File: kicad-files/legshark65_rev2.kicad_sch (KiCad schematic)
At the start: 193 parts, among them J1 ARM JTAG, J2 Conn_01x04, SW1 K2-1187SQ-A4SW-06, SW2 PCM12SMTR, T2 53261-0471, U1 STM32F411CEU6, U2 MCP1700T-3302E/TT, U3 AT24C256C-SSHL-T, Y1 TAXM8M4RFDCET2T

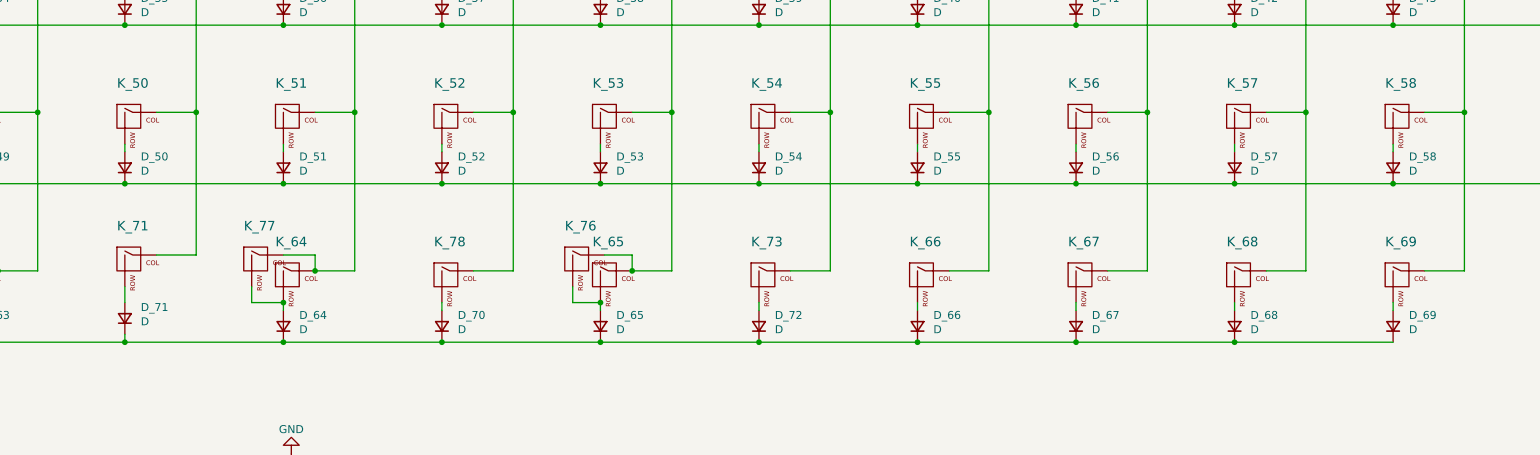
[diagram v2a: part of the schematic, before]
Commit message: Added alternate mods to the right side
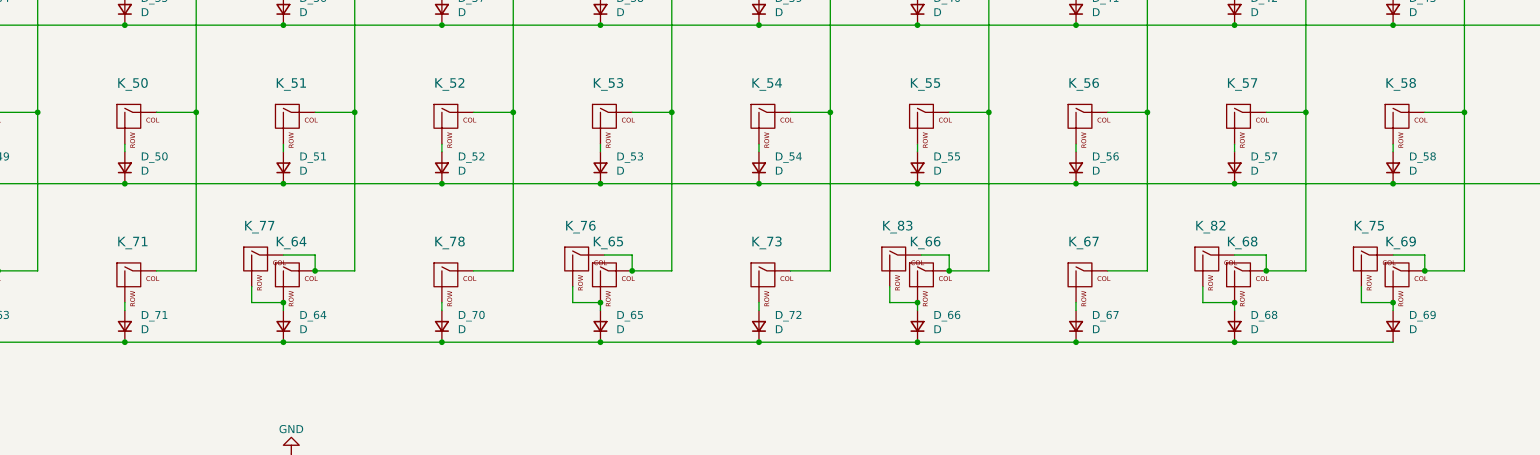
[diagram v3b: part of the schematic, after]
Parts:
- added K_75, K_83: KEYSW, MX_Only:MXOnly-1.5U-NoLED, symbol MX_Alps_Hybrid:MX-NoLED
- added K_82: KEYSW, MX_Only:MXOnly-1U-NoLED, symbol MX_Alps_Hybrid:MX-NoLED
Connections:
- net col10: now also K_83.1 (COL)
- net col12: now also K_82.1 (COL)
- net col13: now also K_75.1 (COL)
- net at D_68.2 (A), K_68.2 (ROW): now also K_82.2 (ROW)
- net at D_66.2 (A), K_66.2 (ROW): now also K_83.2 (ROW)
- net at D_69.2 (A), K_69.2 (ROW): now also K_75.2 (ROW)
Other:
- moved on the sheet: D_71, K_71
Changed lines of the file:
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@@
   (junction (at 223.52 100.33) (diameter 0) (color 0 0 0 0)
   )
+  (junction (at 364.49 130.81) (diameter 0) (color 0 0 0 0)
+  )
   (junction (at 186.69 60.96) (diameter 0) (color 0 0 0 0)
   )
@@
   (junction (at 110.49 35.56) (diameter 0) (color 0 0 0 0)
   )
+  (junction (at 339.09 130.81) (diameter 0) (color 0 0 0 0)
+  )
   (junction (at 191.77 125.73) (diameter 0) (color 0 0 0 0)
   )
@@
   (junction (at 375.92 100.33) (diameter 0) (color 0 0 0 0)
   )
+  (junction (at 369.57 125.73) (diameter 0) (color 0 0 0 0)
+  )
   (junction (at 110.49 60.96) (diameter 0) (color 0 0 0 0)
   )
@@
   (junction (at 313.69 86.36) (diameter 0) (color 0 0 0 0)
   )
+  (junction (at 288.29 130.81) (diameter 0) (color 0 0 0 0)
+  )
   (junction (at 161.29 35.56) (diameter 0) (color 0 0 0 0)
   )
@@
   (junction (at 401.32 49.53) (diameter 0) (color 0 0 0 0)
   )
+  (junction (at 293.37 125.73) (diameter 0) (color 0 0 0 0)
+  )
   (junction (at 135.89 86.36) (diameter 0) (color 0 0 0 0)
   )
@@
   (junction (at 172.72 74.93) (diameter 0) (color 0 0 0 0)
   )
+  (junction (at 344.17 125.73) (diameter 0) (color 0 0 0 0)
+  )
   (junction (at 299.72 74.93) (diameter 0) (color 0 0 0 0)
   )
@@
     (stroke (width 0) (type default))
   )
-  (wire (pts (xy 161.29 128.27) (xy 161.29 130.81))
+  (wire (pts (xy 161.29 130.81) (xy 161.29 132.08))
     (stroke (width 0) (type default))
   )
@@
     (stroke (width 0) (type default))
   )
-  (wire (pts (xy 166.37 123.19) (xy 172.72 123.19))
+  (wire (pts (xy 166.37 125.73) (xy 172.72 125.73))
     (stroke (width 0) (type default))
   )
@@
     (stroke (width 0) (type default))
   )
+  (wire (pts (xy 359.41 128.27) (xy 359.41 130.81))
+    (stroke (width 0) (type default))
+  )
   (wire (pts (xy 198.12 125.73) (xy 198.12 100.33))
     (stroke (width 0) (type default))
@@
     (stroke (width 0) (type default))
   )
+  (wire (pts (xy 283.845 130.81) (xy 288.29 130.81))
+    (stroke (width 0) (type default))
+  )
   (wire (pts (xy 142.24 180.975) (xy 142.24 187.96))
     (stroke (width 0) (type default))
@@
     (stroke (width 0) (type default))
   )
-  (wire (pts (xy 172.72 123.19) (xy 172.72 100.33))
+  (wire (pts (xy 172.72 125.73) (xy 172.72 100.33))
     (stroke (width 0) (type default))
   )
@@
     (stroke (width 0) (type default))
   )
+  (wire (pts (xy 369.57 123.19) (xy 369.57 125.73))
+    (stroke (width 0) (type default))
+  )
   (wire (pts (xy 47.625 259.715) (xy 50.165 259.715))
     (stroke (width 0) (type default))
@@
     (stroke (width 0) (type default))
   )
+  (wire (pts (xy 364.49 123.19) (xy 369.57 123.19))
+    (stroke (width 0) (type default))
+  )
   (wire (pts (xy 267.97 100.33) (xy 274.32 100.33))
     (stroke (width 0) (type default))
@@
     (stroke (width 0) (type default))
   )
+  (wire (pts (xy 334.01 130.81) (xy 339.09 130.81))
+    (stroke (width 0) (type default))
+  )
   (wire (pts (xy 135.89 35.56) (xy 161.29 35.56))
     (stroke (width 0) (type default))
@@
     (stroke (width 0) (type default))
   )
+  (wire (pts (xy 344.17 123.19) (xy 344.17 125.73))
+    (stroke (width 0) (type default))
+  )
   (wire (pts (xy 191.77 283.21) (xy 191.77 285.75))
     (stroke (width 0) (type default))
@@
     (stroke (width 0) (type default))
   )
+  (wire (pts (xy 334.01 128.27) (xy 334.01 130.81))
+    (stroke (width 0) (type default))
+  )
   (wire (pts (xy 344.17 24.13) (xy 350.52 24.13))
     (stroke (width 0) (type default))
@@
     (stroke (width 0) (type default))
   )
+  (wire (pts (xy 283.845 128.27) (xy 283.845 130.81))
+    (stroke (width 0) (type default))
+  )
   (wire (pts (xy 81.28 156.21) (xy 77.47 156.21))
     (stroke (width 0) (type default))
@@
     (stroke (width 0) (type default))
   )
+  (wire (pts (xy 293.37 123.19) (xy 293.37 125.73))
+    (stroke (width 0) (type default))
+  )
   (wire (pts (xy 318.77 100.33) (xy 325.12 100.33))
     (stroke (width 0) (type default))
@@
     (stroke (width 0) (type default))
   )
-  (wire (pts (xy 161.29 135.89) (xy 161.29 137.16))
-    (stroke (width 0) (type default))
-  )
   (wire (pts (xy 191.77 125.73) (xy 198.12 125.73))
     (stroke (width 0) (type default))
@@
     (stroke (width 0) (type default))
   )
+  (wire (pts (xy 359.41 130.81) (xy 364.49 130.81))
+    (stroke (width 0) (type default))
+  )
   (wire (pts (xy 64.77 24.13) (xy 71.12 24.13))
     (stroke (width 0) (type default))
@@
     (stroke (width 0) (type default))
   )
+  (wire (pts (xy 339.09 123.19) (xy 344.17 123.19))
+    (stroke (width 0) (type default))
+  )
   (wire (pts (xy 262.89 137.16) (xy 288.29 137.16))
     (stroke (width 0) (type default))
@@
     (stroke (width 0) (type default))
   )
+  (wire (pts (xy 288.925 123.19) (xy 293.37 123.19))
+    (stroke (width 0) (type default))
+  )
   (wire (pts (xy 204.47 283.21) (xy 204.47 298.45))
     (stroke (width 0) (type default))
@@
     )
   )
-  (symbol (lib_id "MX_Alps_Hybrid:MX-NoLED") (at 162.56 124.46 0) (unit 1)
+  (symbol (lib_id "MX_Alps_Hybrid:MX-NoLED") (at 162.56 127 0) (unit 1)
     (in_bom yes) (on_board yes) (dnp no)
-    (property "Reference" "K_71" (at 162.56 118.5418 0)
+    (property "Reference" "K_71" (at 162.56 121.0818 0)
       (effects (font (size 1.524 1.524)))
     )
-    (property "Value" "KEYSW" (at 162.56 127 0)
+    (property "Value" "KEYSW" (at 162.56 129.54 0)
       (effects (font (size 1.524 1.524)) hide)
     )
-    (property "Footprint" "MX_Only:MXOnly-1U-NoLED" (at 162.56 124.46 0)
+    (property "Footprint" "MX_Only:MXOnly-1U-NoLED" (at 162.56 127 0)
       (effects (font (size 1.524 1.524)) hide)
     )
-    (property "Datasheet" "" (at 162.56 124.46 0)
+    (property "Datasheet" "" (at 162.56 127 0)
       (effects (font (size 1.524 1.524)))
     )
@@
     )
   )
+  (symbol (lib_id "MX_Alps_Hybrid:MX-NoLED") (at 360.68 124.46 0) (unit 1)
+    (in_bom yes) (on_board yes) (dnp no)
+    (property "Reference" "K_75" (at 360.68 118.5418 0)
+      (effects (font (size 1.524 1.524)))
+    )
+    (property "Value" "KEYSW" (at 360.68 127 0)
+      (effects (font (size 1.524 1.524)) hide)
+    )
+    (property "Footprint" "MX_Only:MXOnly-1.5U-NoLED" (at 360.68 124.46 0)
+      (effects (font (size 1.524 1.524)) hide)
+    )
+    (property "Datasheet" "" (at 360.68 124.46 0)
+      (effects (font (size 1.524 1.524)))
+    )
+    (pin "1")
+    (pin "2")
+    (instances
+      (project "legshark65_rev2"
+        (path "/2fcc1073-d3f4-43f9-b3b4-5cee13272705"
+          (reference "K_75") (unit 1)
+        )
+      )
+    )
+  )
   (symbol (lib_id "MX_Alps_Hybrid:MX-NoLED") (at 81.915 124.46 0) (unit 1)
     (in_bom yes) (on_board yes) (dnp no)
@@
     )
   )
-  (symbol (lib_id "Device:D_Small") (at 161.29 133.35 90) (unit 1)
+  (symbol (lib_id "Device:D_Small") (at 161.29 134.62 90) (unit 1)
     (in_bom yes) (on_board yes) (dnp no)
-    (property "Reference" "D_71" (at 163.83 131.572 90)
+    (property "Reference" "D_71" (at 163.83 132.842 90)
       (effects (font (size 1.27 1.27)) (justify right))
     )
-    (property "Value" "D" (at 163.83 133.858 90)
+    (property "Value" "D" (at 163.83 135.128 90)
       (effects (font (size 1.27 1.27)) (justify right))
     )
-    (property "Footprint" "Diode_SMD:D_SOD-523" (at 162.56 140.97 0)
+    (property "Footprint" "Diode_SMD:D_SOD-523" (at 162.56 142.24 0)
       (effects (font (size 1.27 1.27)) hide)
     )
-    (property "Datasheet" "~" (at 162.56 140.97 0)
+    (property "Datasheet" "~" (at 162.56 142.24 0)
       (effects (font (size 1.27 1.27)) hide)
     )
@@
     )
   )
+  (symbol (lib_id "MX_Alps_Hybrid:MX-NoLED") (at 335.28 124.46 0) (unit 1)
+    (in_bom yes) (on_board yes) (dnp no)
+    (property "Reference" "K_82" (at 335.28 118.5418 0)
+      (effects (font (size 1.524 1.524)))
+    )
+    (property "Value" "KEYSW" (at 335.28 127 0)
+      (effects (font (size 1.524 1.524)) hide)
+    )
+    (property "Footprint" "MX_Only:MXOnly-1U-NoLED" (at 335.28 124.46 0)
+      (effects (font (size 1.524 1.524)) hide)
+    )
+    (property "Datasheet" "" (at 335.28 124.46 0)
+      (effects (font (size 1.524 1.524)))
+    )
+    (pin "1")
+    (pin "2")
+    (instances
+      (project "legshark65_rev2"
+        (path "/2fcc1073-d3f4-43f9-b3b4-5cee13272705"
+          (reference "K_82") (unit 1)
+        )
+      )
+    )
+  )
   (symbol (lib_id "MX_Alps_Hybrid:MX-NoLED") (at 187.96 127 0) (unit 1)
     (in_bom yes) (on_board yes) (dnp no)
@@
         )
       )
+    )
+  )
+  (symbol (lib_id "MX_Alps_Hybrid:MX-NoLED") (at 285.115 124.46 0) (unit 1)
+    (in_bom yes) (on_board yes) (dnp no)
+    (property "Reference" "K_83" (at 285.115 118.5418 0)
+      (effects (font (size 1.524 1.524)))
+    )
+    (property "Value" "KEYSW" (at 285.115 127 0)
+      (effects (font (size 1.524 1.524)) hide)
+    )
+    (property "Footprint" "MX_Only:MXOnly-1.5U-NoLED" (at 285.115 124.46 0)
+      (effects (font (size 1.524 1.524)) hide)
+    )
+    (property "Datasheet" "" (at 285.115 124.46 0)
+      (effects (font (size 1.524 1.524)))
+    )
+    (pin "1")
+    (pin "2")
+    (instances
+      (project "legshark65_rev2"
+        (path "/2fcc1073-d3f4-43f9-b3b4-5cee13272705"
+          (reference "K_83") (unit 1)
+        )
+      )

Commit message: Added 3U stabs to the 7U footprint for even more layout support
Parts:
- K_78: footprint MX_Only:MXOnly-7U-ReversedStabilizers-NoLED -> Legshark:Legshark_MXOnly-7U-3U-ReversedStabilizers-NoLED
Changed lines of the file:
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@@
       (effects (font (size 1.524 1.524)) hide)
     )
-    (property "Footprint" "MX_Only:MXOnly-7U-ReversedStabilizers-NoLED" (at 213.36 127 0)
+    (property "Footprint" "Legshark:Legshark_MXOnly-7U-3U-ReversedStabilizers-NoLED" (at 213.36 127 0)
       (effects (font (size 1.524 1.524)) hide)
     )

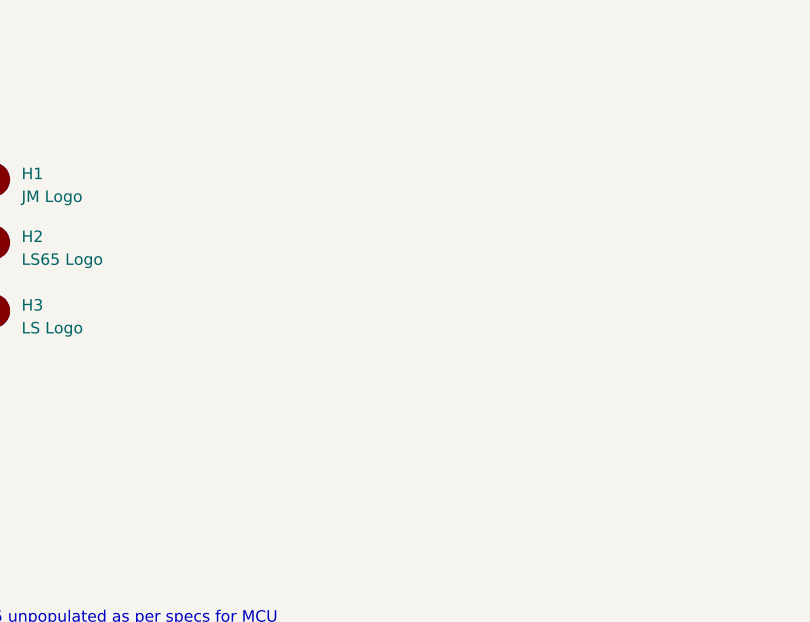
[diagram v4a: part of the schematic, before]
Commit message: added mounting holes with clearence
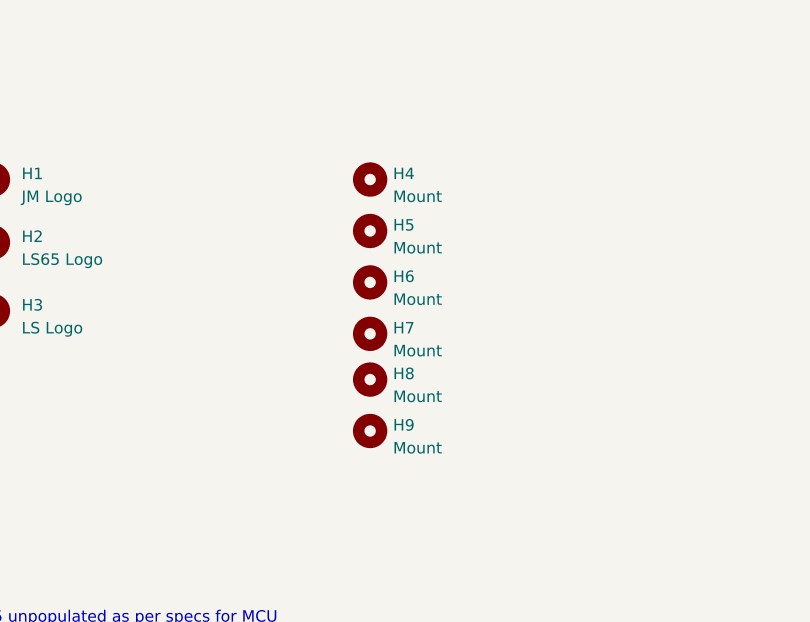
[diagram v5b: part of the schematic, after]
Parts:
- added H4, H5, H6, H7, H8, H9: Mount, MountingHole:MountingHole_3.2mm_M3_ISO14580, symbol Mechanical:MountingHole
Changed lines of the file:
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@@
     )
   )
+  (symbol (lib_id "Mechanical:MountingHole") (at 285.75 191.77 0) (unit 1)
+    (in_bom yes) (on_board yes) (dnp no) (fields_autoplaced)
+    (property "Reference" "H7" (at 288.29 191.135 0)
+      (effects (font (size 1.27 1.27)) (justify left))
+    )
+    (property "Value" "Mount" (at 288.29 193.675 0)
+      (effects (font (size 1.27 1.27)) (justify left))
+    )
+    (property "Footprint" "MountingHole:MountingHole_3.2mm_M3_ISO14580" (at 285.75 191.77 0)
+      (effects (font (size 1.27 1.27)) hide)
+    )
+    (property "Datasheet" "~" (at 285.75 191.77 0)
+      (effects (font (size 1.27 1.27)) hide)
+    )
+    (instances
+      (project "legshark65_rev2"
+        (path "/2fcc1073-d3f4-43f9-b3b4-5cee13272705"
+          (reference "H7") (unit 1)
+        )
+      )
+      (project "legshark65_rev1"
+        (path "/9ddf6dc5-8b5e-413a-9b25-d1d5a5a60469"
+          (reference "H3") (unit 1)
+        )
+      )
+    )
+  )
   (symbol (lib_id "Device:D_Small") (at 85.09 134.62 90) (unit 1)
     (in_bom yes) (on_board yes) (dnp no)
@@
     )
   )
+  (symbol (lib_id "Mechanical:MountingHole") (at 285.75 202.565 0) (unit 1)
+    (in_bom yes) (on_board yes) (dnp no) (fields_autoplaced)
+    (property "Reference" "H9" (at 288.29 201.93 0)
+      (effects (font (size 1.27 1.27)) (justify left))
+    )
+    (property "Value" "Mount" (at 288.29 204.47 0)
+      (effects (font (size 1.27 1.27)) (justify left))
+    )
+    (property "Footprint" "MountingHole:MountingHole_3.2mm_M3_ISO14580" (at 285.75 202.565 0)
+      (effects (font (size 1.27 1.27)) hide)
+    )
+    (property "Datasheet" "~" (at 285.75 202.565 0)
+      (effects (font (size 1.27 1.27)) hide)
+    )
+    (instances
+      (project "legshark65_rev2"
+        (path "/2fcc1073-d3f4-43f9-b3b4-5cee13272705"
+          (reference "H9") (unit 1)
+        )
+      )
+      (project "legshark65_rev1"
+        (path "/9ddf6dc5-8b5e-413a-9b25-d1d5a5a60469"
+          (reference "H3") (unit 1)
+        )
+      )
+    )
+  )
   (symbol (lib_id "MX_Alps_Hybrid:MX-NoLED") (at 289.56 25.4 0) (unit 1)
     (in_bom yes) (on_board yes) (dnp no)
@@
     )
   )
+  (symbol (lib_id "Mechanical:MountingHole") (at 285.75 196.85 0) (unit 1)
+    (in_bom yes) (on_board yes) (dnp no) (fields_autoplaced)
+    (property "Reference" "H8" (at 288.29 196.215 0)
+      (effects (font (size 1.27 1.27)) (justify left))
+    )
+    (property "Value" "Mount" (at 288.29 198.755 0)
+      (effects (font (size 1.27 1.27)) (justify left))
+    )
+    (property "Footprint" "MountingHole:MountingHole_3.2mm_M3_ISO14580" (at 285.75 196.85 0)
+      (effects (font (size 1.27 1.27)) hide)
+    )
+    (property "Datasheet" "~" (at 285.75 196.85 0)
+      (effects (font (size 1.27 1.27)) hide)
+    )
+    (instances
+      (project "legshark65_rev2"
+        (path "/2fcc1073-d3f4-43f9-b3b4-5cee13272705"
+          (reference "H8") (unit 1)
+        )
+      )
+      (project "legshark65_rev1"
+        (path "/9ddf6dc5-8b5e-413a-9b25-d1d5a5a60469"
+          (reference "H3") (unit 1)
+        )
+      )
+    )
+  )
   (symbol (lib_id "MX_Alps_Hybrid:MX-NoLED") (at 289.56 76.2 0) (unit 1)
     (in_bom yes) (on_board yes) (dnp no)
@@
     )
   )
+  (symbol (lib_id "Mechanical:MountingHole") (at 285.75 186.055 0) (unit 1)
+    (in_bom yes) (on_board yes) (dnp no) (fields_autoplaced)
+    (property "Reference" "H6" (at 288.29 185.42 0)
+      (effects (font (size 1.27 1.27)) (justify left))
+    )
+    (property "Value" "Mount" (at 288.29 187.96 0)
+      (effects (font (size 1.27 1.27)) (justify left))
+    )
+    (property "Footprint" "MountingHole:MountingHole_3.2mm_M3_ISO14580" (at 285.75 186.055 0)
+      (effects (font (size 1.27 1.27)) hide)
+    )
+    (property "Datasheet" "~" (at 285.75 186.055 0)
+      (effects (font (size 1.27 1.27)) hide)
+    )
+    (instances
+      (project "legshark65_rev2"
+        (path "/2fcc1073-d3f4-43f9-b3b4-5cee13272705"
+          (reference "H6") (unit 1)
+        )
+      )
+      (project "legshark65_rev1"
+        (path "/9ddf6dc5-8b5e-413a-9b25-d1d5a5a60469"
+          (reference "H3") (unit 1)
+        )
+      )
+    )
+  )
   (symbol (lib_id "MX_Alps_Hybrid:MX-NoLED") (at 340.36 25.4 0) (unit 1)
     (in_bom yes) (on_board yes) (dnp no)
@@
     )
   )
+  (symbol (lib_id "Mechanical:MountingHole") (at 285.75 174.625 0) (unit 1)
+    (in_bom yes) (on_board yes) (dnp no) (fields_autoplaced)
+    (property "Reference" "H4" (at 288.29 173.99 0)
+      (effects (font (size 1.27 1.27)) (justify left))
+    )
+    (property "Value" "Mount" (at 288.29 176.53 0)
+      (effects (font (size 1.27 1.27)) (justify left))
+    )
+    (property "Footprint" "MountingHole:MountingHole_3.2mm_M3_ISO14580" (at 285.75 174.625 0)
+      (effects (font (size 1.27 1.27)) hide)
+    )
+    (property "Datasheet" "~" (at 285.75 174.625 0)
+      (effects (font (size 1.27 1.27)) hide)
+    )
+    (instances
+      (project "legshark65_rev2"
+        (path "/2fcc1073-d3f4-43f9-b3b4-5cee13272705"
+          (reference "H4") (unit 1)
+        )
+      )
+      (project "legshark65_rev1"
+        (path "/9ddf6dc5-8b5e-413a-9b25-d1d5a5a60469"
+          (reference "H3") (unit 1)
+        )
+      )
+    )
+  )
   (symbol (lib_id "Device:D_Small") (at 59.69 58.42 90) (unit 1)
     (in_bom yes) (on_board yes) (dnp no)
@@
         )
       )
+    )
+  )
+  (symbol (lib_id "Mechanical:MountingHole") (at 285.75 180.34 0) (unit 1)
+    (in_bom yes) (on_board yes) (dnp no) (fields_autoplaced)
+    (property "Reference" "H5" (at 288.29 179.705 0)
+      (effects (font (size 1.27 1.27)) (justify left))
+    )
+    (property "Value" "Mount" (at 288.29 182.245 0)
+      (effects (font (size 1.27 1.27)) (justify left))
+    )
+    (property "Footprint" "MountingHole:MountingHole_3.2mm_M3_ISO14580" (at 285.75 180.34 0)
+      (effects (font (size 1.27 1.27)) hide)
+    )
+    (property "Datasheet" "~" (at 285.75 180.34 0)
+      (effects (font (size 1.27 1.27)) hide)
+    )
+    (instances
+      (project "legshark65_rev2"
+        (path "/2fcc1073-d3f4-43f9-b3b4-5cee13272705"
+          (reference "H5") (unit 1)
+        )
+      )
+      (project "legshark65_rev1"
+        (path "/9ddf6dc5-8b5e-413a-9b25-d1d5a5a60469"
+          (reference "H3") (unit 1)
+        )
+      )
